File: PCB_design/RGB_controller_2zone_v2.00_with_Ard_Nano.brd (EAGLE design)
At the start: 75.9 x 63.5 mm, 25 parts, among them Q1 IRF512, Q2 IRF512, Q3 IRF512, Q4 IRF512, Q5 IRF512, Q6 IRF512

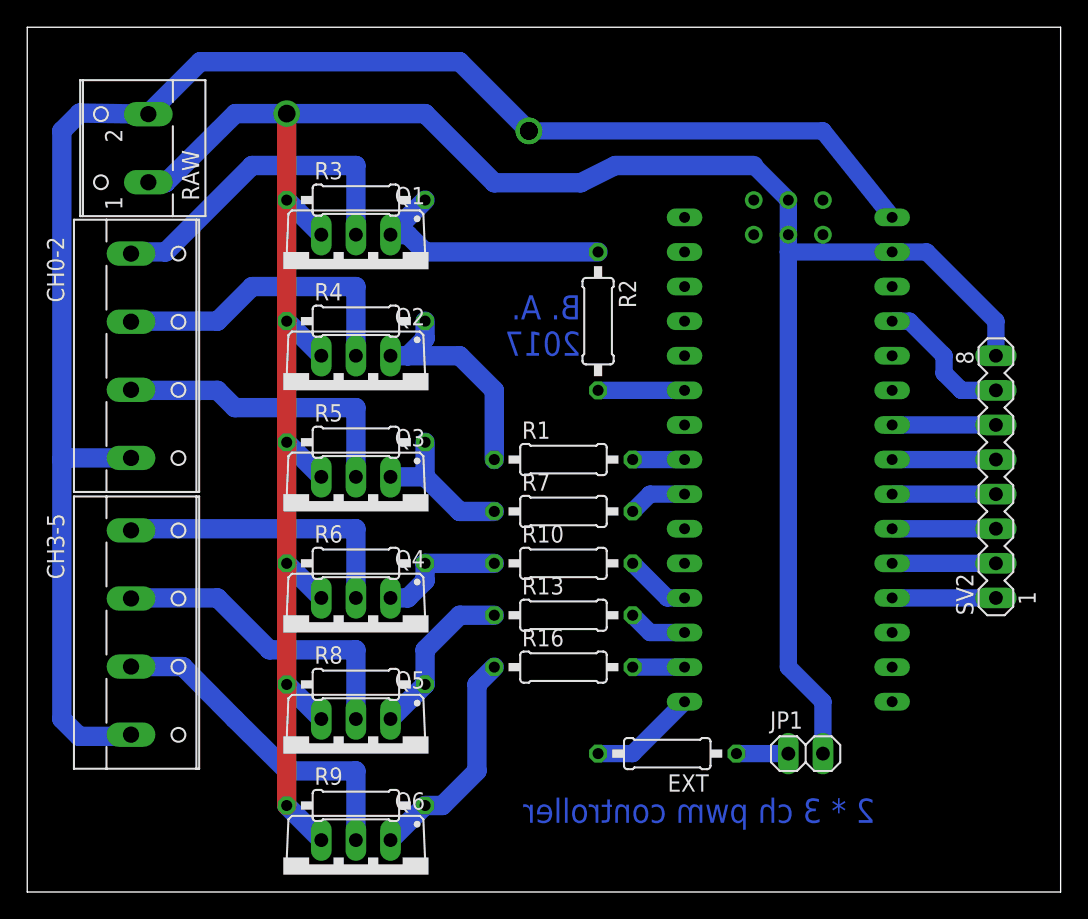
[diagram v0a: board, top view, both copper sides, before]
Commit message: Update PCB for using arduino nano
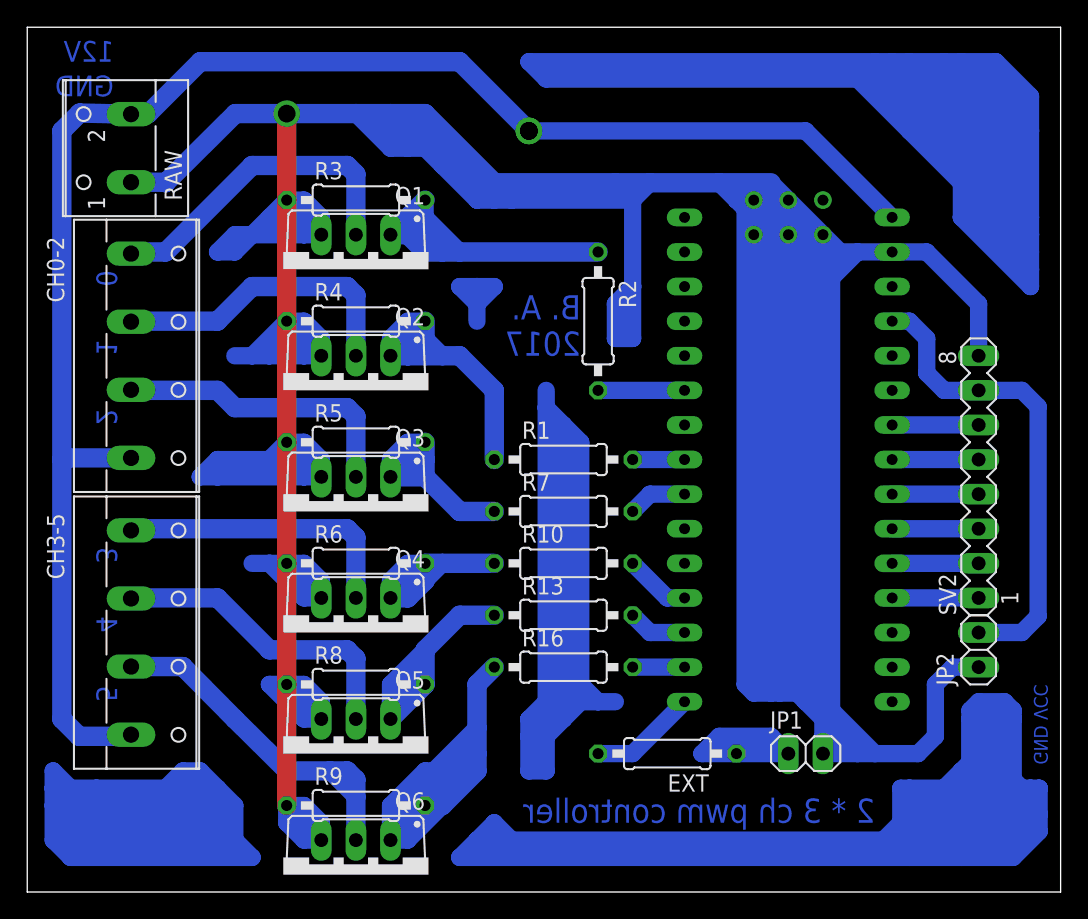
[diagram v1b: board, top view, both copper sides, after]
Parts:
- added JP2: (no value), pinhead:1X02
- moved SV2 1.27 mm to (69.8, 30.5)
- moved RAW 1.27 mm to (6.35, 54.6)
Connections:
- net GND: now also JP2.1
- net VCC: now also JP2.2
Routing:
- net GND: track 186.5 -> 585.1 mm
- net PH1: track 0.00 -> 191.9 mm
- net PH3: track 0.00 -> 184.4 mm
- net PH2: track 0.00 -> 90.6 mm
- net PH4: track 0.00 -> 79.8 mm
- net GATE_6: track 16.6 -> 54.8 mm
- net VCC: track 10.5 -> 35.1 mm
- net GATE_2: track 16.8 -> 29.1 mm
- net GATE_5: track 12.3 -> 23.3 mm
- net GATE_1: track 19.4 -> 30.4 mm
- net N$2: track 3.81 -> 13.8 mm
- net GATE_4: track 9.42 -> 19.1 mm
- net N$3: track 0.00 -> 8.67 mm
- net GATE_3: track 11.2 -> 19.9 mm
- net N$6: track 0.00 -> 3.59 mm
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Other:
- board text added: "0"
- board text added: "1"
- board text added: "12V"
- board text added: "2"
- board text added: "3"
- board text added: "4"
- board text added: "5"
- board text added: "GND"
- board text added: "GND VCC"
